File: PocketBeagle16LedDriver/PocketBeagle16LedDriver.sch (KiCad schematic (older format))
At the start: 16 parts, among them J1 RJ45, J2 RJ45, P1 POCKETBEAGLE-P1, P2 POCKETBEAGLE-P2, T1 + 15 in -, T2 + 15 out -, U1 TCAN332DR, U2 SN65HVD233-HT

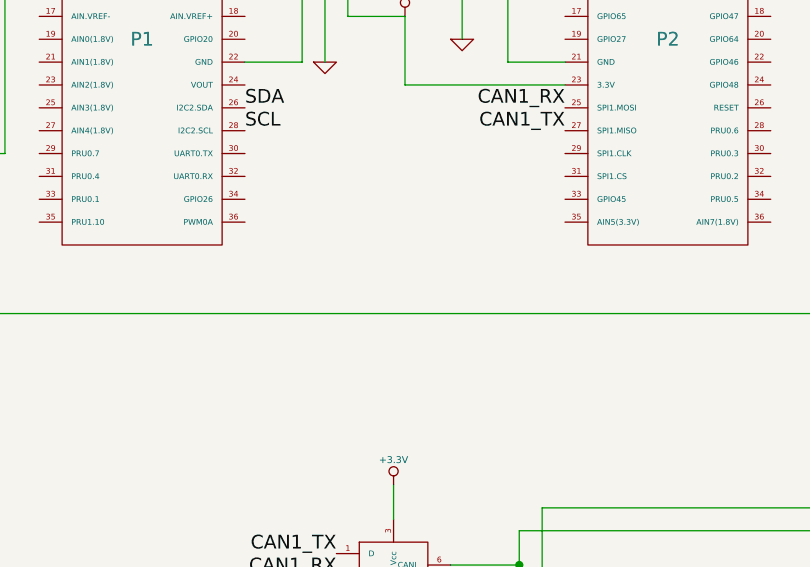
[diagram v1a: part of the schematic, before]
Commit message: Update PocketBeagle16LedDriver to use 12V for the LEDs.
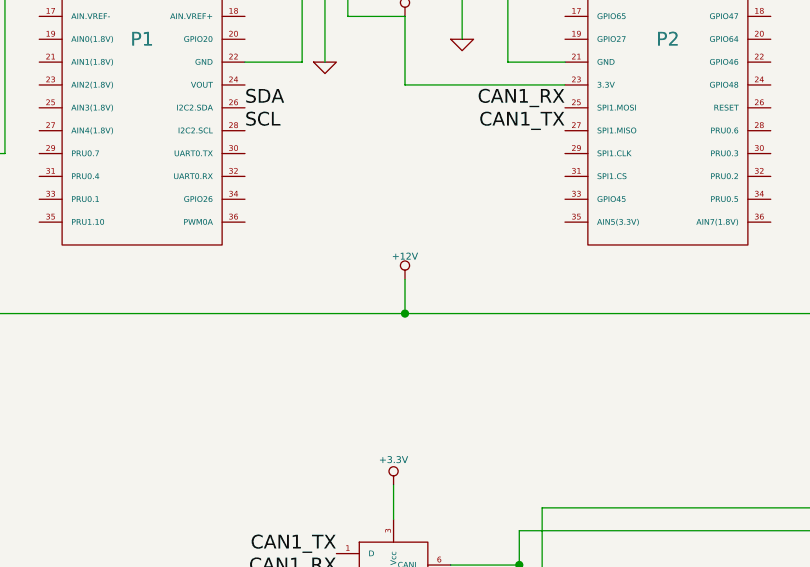
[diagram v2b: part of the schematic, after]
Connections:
- net Power Supply/12-15 Volt input renamed +12V
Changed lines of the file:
@@
 Sheet 1 3
 Title ""
-Date "7 mar 2019"
+Date "28 mar 2019"
 Rev ""
 Comp ""
@@
 Text Label 2800 6300 0    60   ~ 0
 SDA
+$Comp
+L +12V #PWR014
+U 1 1 5C9C29E0
+P 4000 3600
+F 0 "#PWR014" H 4000 3550 20  0001 C CNN
+F 1 "+12V" H 4000 3700 30  0000 C CNN
+F 2 "" H 4000 3600 60  0000 C CNN
+F 3 "" H 4000 3600 60  0000 C CNN
+	1    4000 3600
+	1    0    0    -1
+$EndComp
+Wire Wire Line
+	4000 3600 4000 3750
+Connection ~ 4000 3750
 $EndSCHEMATC

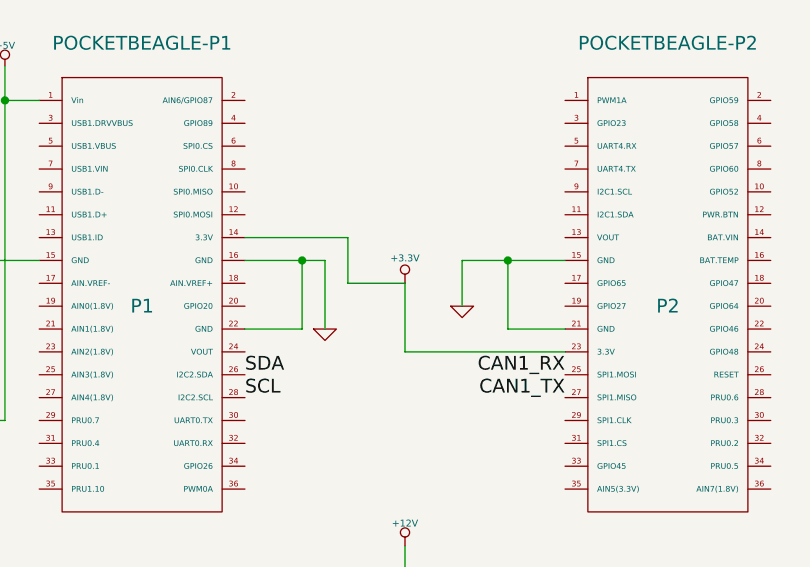
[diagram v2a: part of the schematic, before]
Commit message: Move from I2C2 to I2C1 (reserve I2C2 for eeprom).
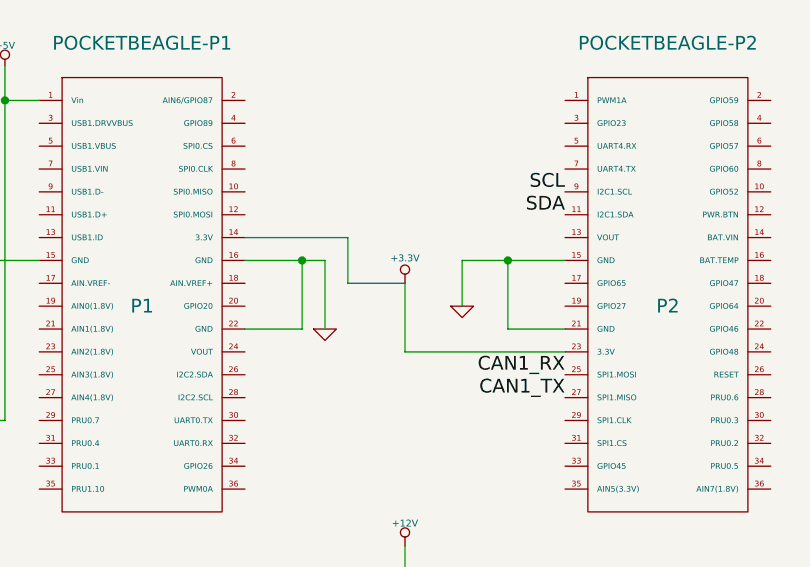
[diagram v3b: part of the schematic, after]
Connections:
- net SCL: now also P2.9 (I2C1.SCL); no longer P1.28 (I2C2.SCL)
- net SDA: now also P2.11 (I2C1.SDA); no longer P1.26 (I2C2.SDA)
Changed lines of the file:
@@
 Sheet 1 3
 Title ""
-Date "28 mar 2019"
+Date "8 jul 2019"
 Rev ""
 Comp ""
@@
 	7100 3750 7100 3400
 Connection ~ 7100 3400
-Text Label 3300 2850 0    60   ~ 0
+Text Label 4700 2150 2    60   ~ 0
 SDA
-Text Label 3300 2950 0    60   ~ 0
+Text Label 4700 2050 2    60   ~ 0
 SCL
 $Sheet

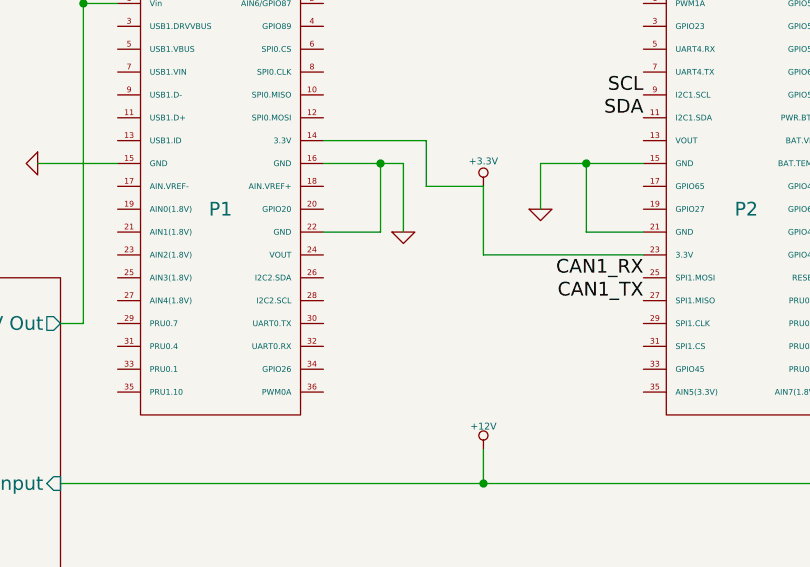
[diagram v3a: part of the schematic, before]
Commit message: Add Console headers to all Pocket Beagle boards.
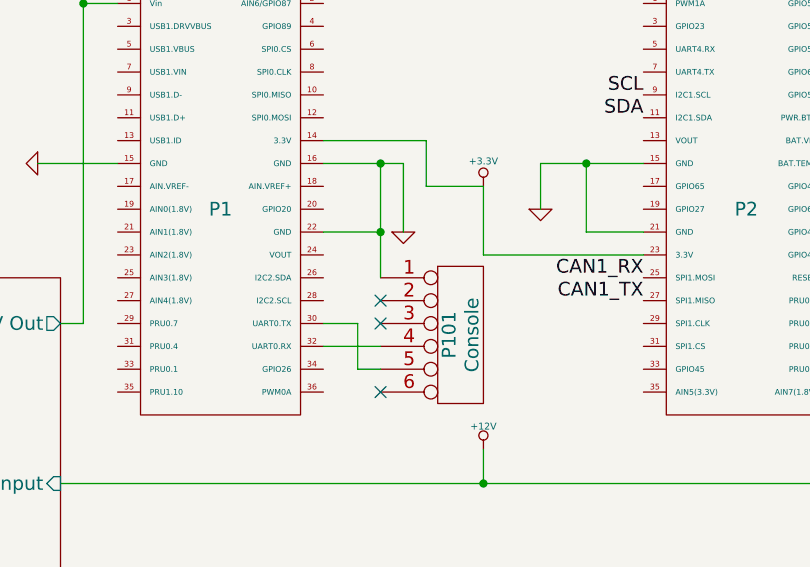
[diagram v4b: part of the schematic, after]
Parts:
- added P101: Console, symbol CONN_6
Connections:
- net GND: now also P101.1
- net at P1.30 (UART0.TX): now also P101.5
- net at P1.32 (UART0.RX): now also P101.4
- no-connect marks 2 -> 5
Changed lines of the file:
@@
 	3300 2650 3550 2650
 Wire Wire Line
-	3550 2650 3550 2350
+	3550 2350 3550 2850
 Connection ~ 3550 2350
 Wire Wire Line
@@
 	4000 3600 4000 3750
 Connection ~ 4000 3750
+$Comp
+L CONN_6 P101
+U 1 1 5D23CD9C
+P 3900 3100
+F 0 "P101" V 3850 3100 60  0000 C CNN
+F 1 "Console" V 3950 3100 60  0000 C CNN
+F 2 "" H 3900 3100 60  0000 C CNN
+F 3 "" H 3900 3100 60  0000 C CNN
+	1    3900 3100
+	1    0    0    -1
+$EndComp
+Wire Wire Line
+	3300 3150 3550 3150
+Wire Wire Line
+	3550 3250 3450 3250
+Wire Wire Line
+	3450 3250 3450 3050
+Wire Wire Line
+	3450 3050 3300 3050
+Connection ~ 3550 2650
+NoConn ~ 3550 2950
+NoConn ~ 3550 3050
+NoConn ~ 3550 3350
 $EndSCHEMATC
